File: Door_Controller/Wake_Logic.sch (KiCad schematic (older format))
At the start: 0 parts

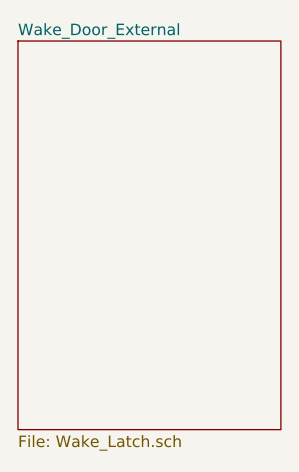
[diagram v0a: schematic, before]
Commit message: complete wake-latch subsheet
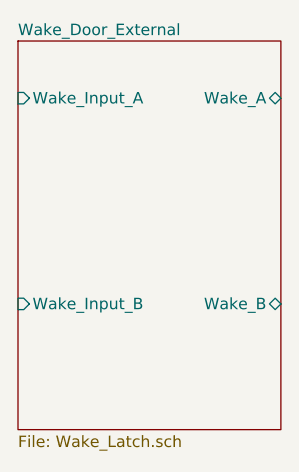
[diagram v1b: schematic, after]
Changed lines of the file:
@@
 F0 "Wake_Door_External" 50
 F1 "Wake_Latch.sch" 50
+F2 "Wake_Input_A" I L 1550 1600 50
+F3 "Wake_Input_B" I L 1550 2500 50
+F4 "Wake_A" B R 2700 1600 50
+F5 "Wake_B" B R 2700 2500 50
 $EndSheet
 $EndSCHEMATC

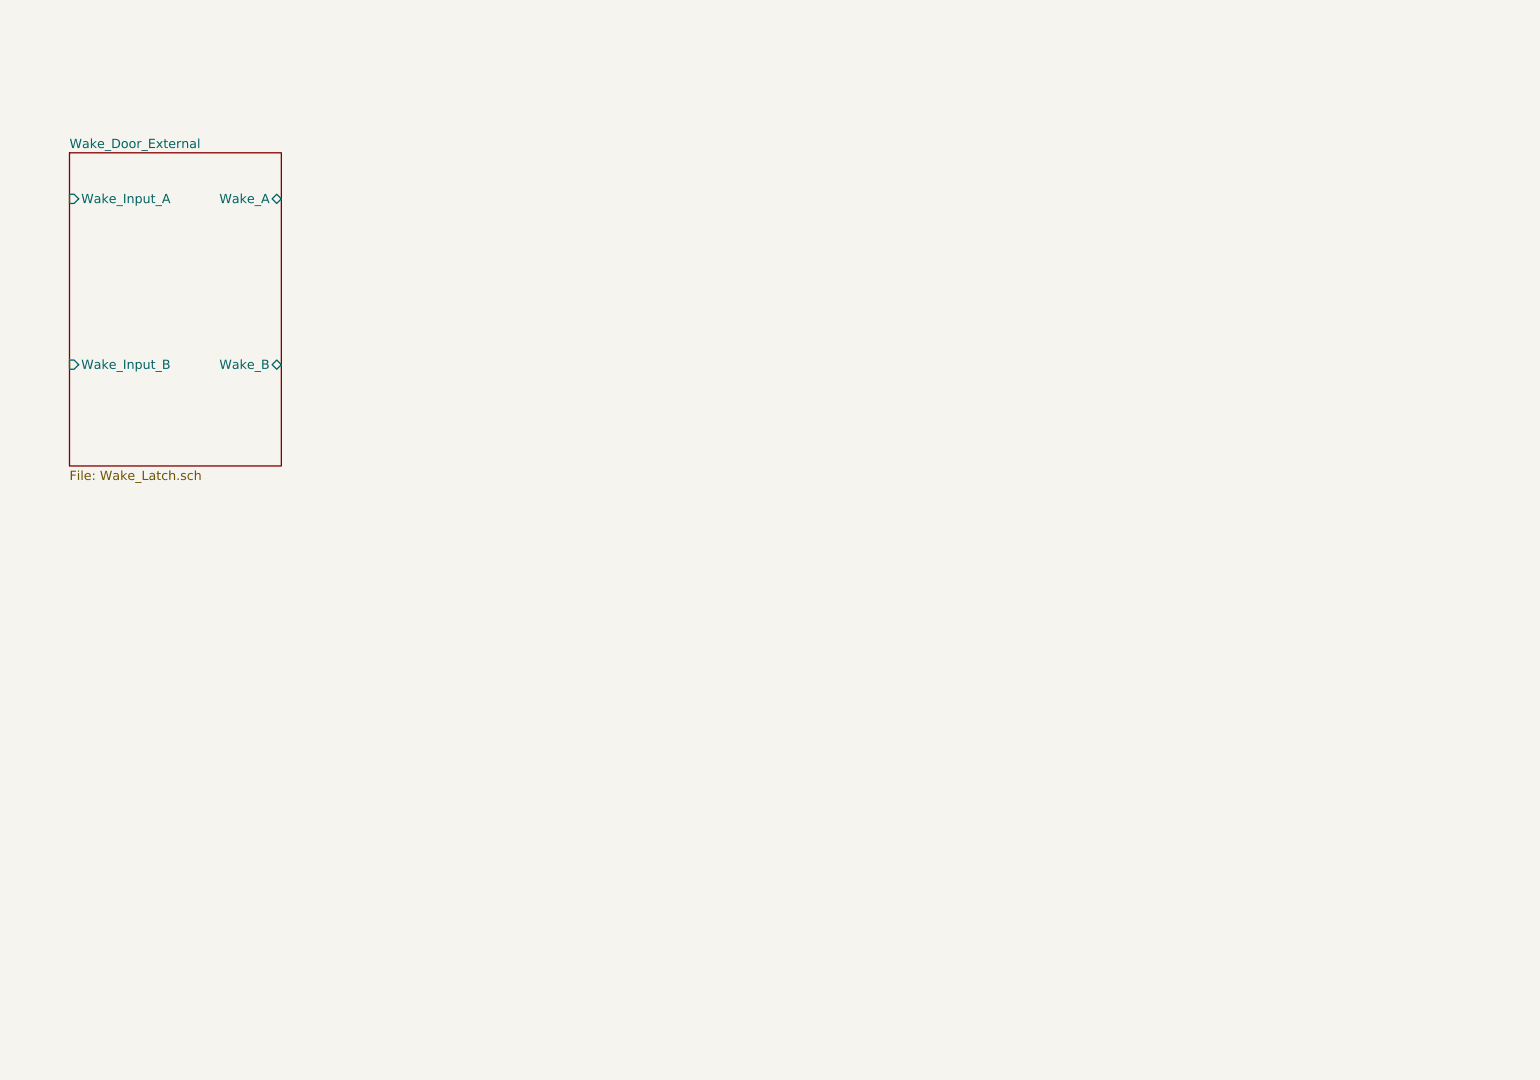
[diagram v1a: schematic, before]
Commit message: Add wake inputs
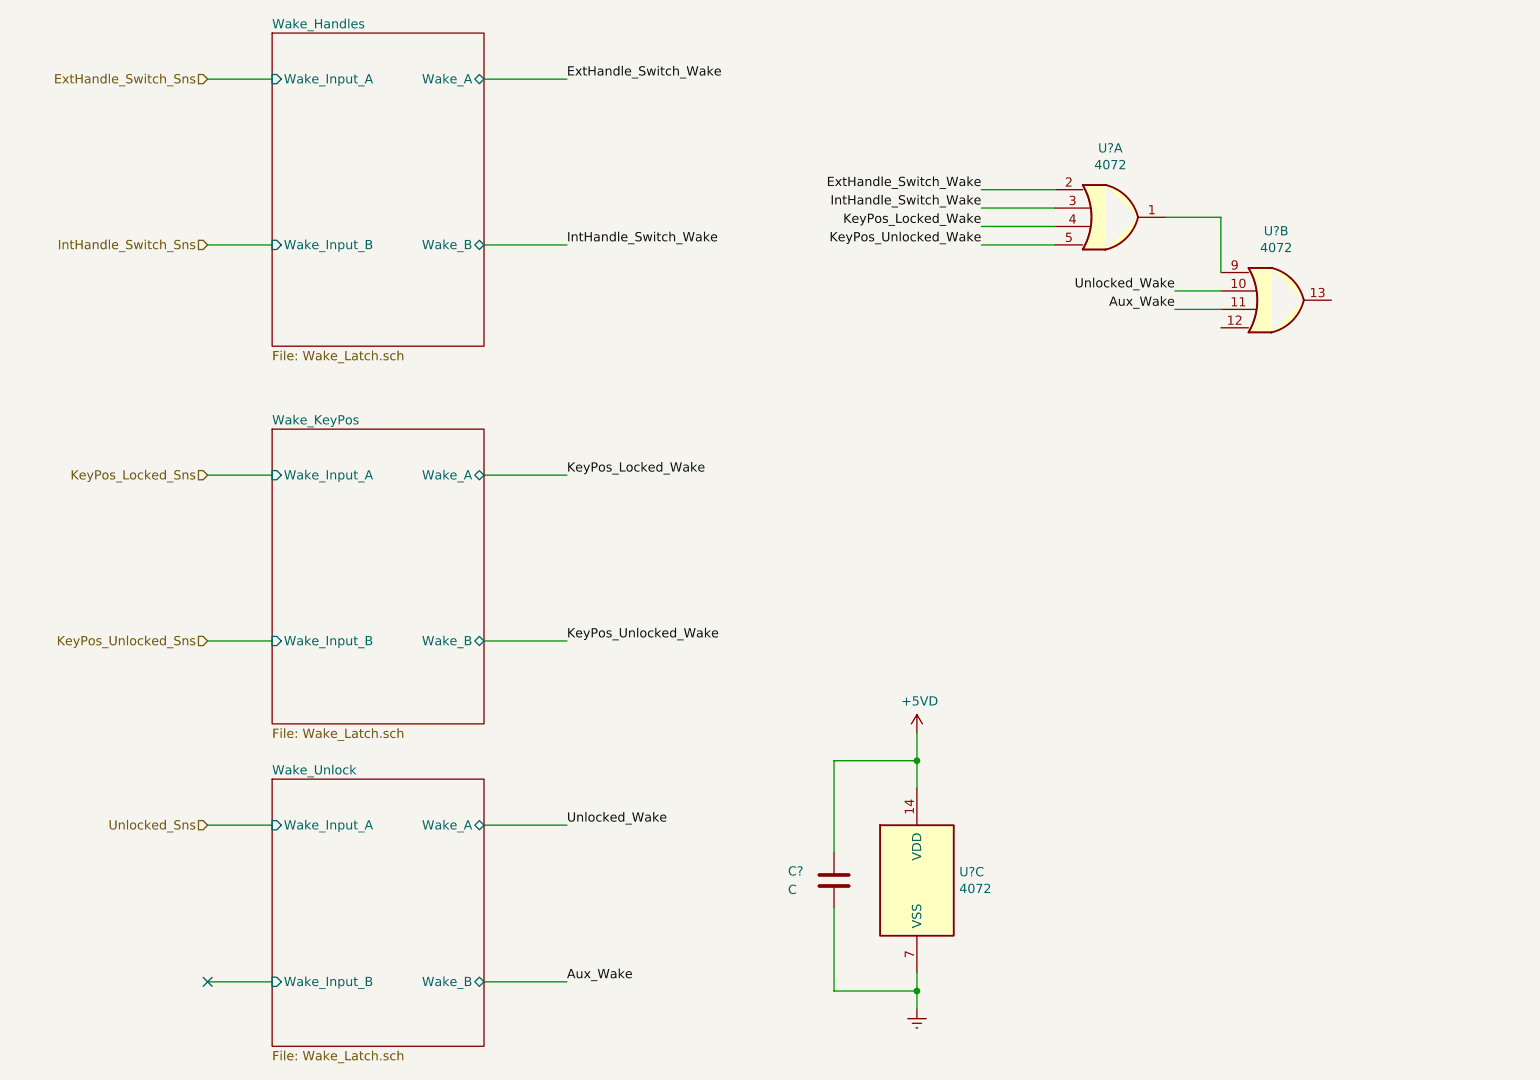
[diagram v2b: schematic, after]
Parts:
- added C?: C, symbol Device:C
- added U? (x3): 4072, symbol 4xxx:4072
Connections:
- new net: U?.1, U?.9
- new net +5VD: C?.1, U?.14 (VDD)
- new net Aux_Wake: U?.11
- new net Earth: C?.2, U?.7 (VSS)
- new net ExtHandle_Switch_Wake: U?.2
- new net IntHandle_Switch_Wake: U?.3
- new net KeyPos_Locked_Wake: U?.4
- new net KeyPos_Unlocked_Wake: U?.5
- new net Unlocked_Wake: U?.10
- no-connect marks 0 -> 1
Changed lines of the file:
@@
 $Descr A4 11693 8268
 encoding utf-8
-Sheet 13 14
+Sheet 13 16
 Title ""
 Date ""
@@
 $EndDescr
 $Sheet
-S 1550 1350 1150 1700
+S 2650 700  1150 1700
 U 60BD8C71
-F0 "Wake_Door_External" 50
+F0 "Wake_Handles" 50
 F1 "Wake_Latch.sch" 50
-F2 "Wake_Input_A" I L 1550 1600 50
-F3 "Wake_Input_B" I L 1550 2500 50
-F4 "Wake_A" B R 2700 1600 50
-F5 "Wake_B" B R 2700 2500 50
+F2 "Wake_Input_A" I L 2650 950 50
+F3 "Wake_Input_B" I L 2650 1850 50
+F4 "Wake_A" B R 3800 950 50
+F5 "Wake_B" B R 3800 1850 50
 $EndSheet
+Text HLabel 2300 950  0    50   Input ~ 0
+ExtHandle_Switch_Sns
+Text HLabel 2300 1850 0    50   Input ~ 0
+IntHandle_Switch_Sns
+Wire Wire Line
+	2300 1850 2650 1850
+Wire Wire Line
+	2300 950  2650 950
+$Sheet
+S 2650 2850 1150 1600
+U 613ABD4B
+F0 "Wake_KeyPos" 50
+F1 "Wake_Latch.sch" 50
+F2 "Wake_Input_A" I L 2650 3100 50
+F3 "Wake_Input_B" I L 2650 4000 50
+F4 "Wake_A" B R 3800 3100 50
+F5 "Wake_B" B R 3800 4000 50
+$EndSheet
+Text HLabel 2300 3100 0    50   Input ~ 0
+KeyPos_Locked_Sns
+Text HLabel 2300 4000 0    50   Input ~ 0
+KeyPos_Unlocked_Sns
+Wire Wire Line
+	2300 4000 2650 4000
+Wire Wire Line
+	2300 3100 2650 3100
+$Sheet
+S 2650 4750 1150 1450
+U 613AC461
+F0 "Wake_Unlock" 50
+F1 "Wake_Latch.sch" 50
+F2 "Wake_Input_A" I L 2650 5000 50
+F3 "Wake_Input_B" I L 2650 5850 50
+F4 "Wake_A" B R 3800 5000 50
+F5 "Wake_B" B R 3800 5850 50
+$EndSheet
+Text HLabel 2300 5000 0    50   Input ~ 0
+Unlocked_Sns
+Wire Wire Line
+	2300 5000 2650 5000
+NoConn ~ 2300 5850
+Wire Wire Line
+	2300 5850 2650 5850
+$Comp
+L 4xxx:4072 U?
+U 1 1 613AD850
+P 7200 1700
+F 0 "U?" H 7200 2075 50  0000 C CNN
+F 1 "4072" H 7200 1984 50  0000 C CNN
+F 2 "" H 7200 1700 50  0001 C CNN
+F 3 "http://www.intersil.com/content/dam/Intersil/documents/cd40/cd4071bms-72bms-75bms.pdf" H 7200 1700 50  0001 C CNN
+	1    7200 1700
+	1    0    0    -1
+$EndComp
+$Comp
+L 4xxx:4072 U?
+U 2 1 613B08A5
+P 8100 2150
+F 0 "U?" H 8100 2525 50  0000 C CNN
+F 1 "4072" H 8100 2434 50  0000 C CNN
+F 2 "" H 8100 2150 50  0001 C CNN
+F 3 "http://www.intersil.com/content/dam/Intersil/documents/cd40/cd4071bms-72bms-75bms.pdf" H 8100 2150 50  0001 C CNN
+	2    8100 2150
+	1    0    0    -1
+$EndComp
+$Comp
+L 4xxx:4072 U?
+U 3 1 613B0DB9
+P 6150 5300
+F 0 "U?" H 6380 5346 50  0000 L CNN
+F 1 "4072" H 6380 5255 50  0000 L CNN
+F 2 "" H 6150 5300 50  0001 C CNN
+F 3 "http://www.intersil.com/content/dam/Intersil/documents/cd40/cd4071bms-72bms-75bms.pdf" H 6150 5300 50  0001 C CNN
+	3    6150 5300
+	1    0    0    -1
+$EndComp
+$Comp
+L power:Earth #PWR?
+U 1 1 613B34D8
+P 6150 6000
+F 0 "#PWR?" H 6150 5750 50  0001 C CNN
+F 1 "Earth" H 6150 5850 50  0001 C CNN
+F 2 "" H 6150 6000 50  0001 C CNN
+F 3 "~" H 6150 6000 50  0001 C CNN
+	1    6150 6000
+	1    0    0    -1
+$EndComp
+$Comp
+L power:+5VD #PWR?
+U 1 1 613B3FE3
+P 6150 4500
+F 0 "#PWR?" H 6150 4350 50  0001 C CNN
+F 1 "+5VD" H 6165 4673 50  0000 C CNN
+F 2 "" H 6150 4500 50  0001 C CNN
+F 3 "" H 6150 4500 50  0001 C CNN
+	1    6150 4500
+	1    0    0    -1
+$EndComp
+$Comp
+L Device:C C?
+U 1 1 613B4A82
+P 5700 5300
+F 0 "C?" H 5450 5350 50  0000 L CNN
+F 1 "C" H 5450 5250 50  0000 L CNN
+F 2 "" H 5738 5150 50  0001 C CNN
+F 3 "~" H 5700 5300 50  0001 C CNN
+	1    5700 5300
+	1    0    0    -1
+$EndComp
+Wire Wire Line
+	6150 4800 6150 4650
+Wire Wire Line
+	6150 5800 6150 5900
+Wire Wire Line
+	5700 5450 5700 5900
+Wire Wire Line
+	5700 5900 6150 5900
+Connection ~ 6150 5900
+Wire Wire Line
+	6150 5900 6150 6000
+Wire Wire Line
+	5700 5150 5700 4650
+Wire Wire Line
+	5700 4650 6150 4650
+Connection ~ 6150 4650
+Wire Wire Line
+	6150 4650 6150 4500
+Text Label 4250 950  0    50   ~ 0
+ExtHandle_Switch_Wake
+Text Label 4250 1850 0    50   ~ 0
+IntHandle_Switch_Wake
+Text Label 4250 3100 0    50   ~ 0
+KeyPos_Locked_Wake
+Text Label 4250 4000 0    50   ~ 0
+KeyPos_Unlocked_Wake
+Text Label 4250 5000 0    50   ~ 0
+Unlocked_Wake
+Text Label 4250 5850 0    50   ~ 0
+Aux_Wake
+Wire Wire Line
+	4250 950  3800 950
+Wire Wire Line
+	4250 1850 3800 1850
+Wire Wire Line
+	4250 3100 3800 3100
+Wire Wire Line
+	3800 4000 4250 4000
+Wire Wire Line
+	3800 5000 4250 5000
+Wire Wire Line
+	3800 5850 4250 5850
+Text Label 6500 1550 2    50   ~ 0
+ExtHandle_Switch_Wake
+Text Label 6500 1650 2    50   ~ 0
+IntHandle_Switch_Wake
+Text Label 6500 1750 2    50   ~ 0
+KeyPos_Locked_Wake
+Text Label 6500 1850 2    50   ~ 0
+KeyPos_Unlocked_Wake
+Text Label 7550 2200 2    50   ~ 0
+Aux_Wake
+Wire Wire Line
+	6900 1550 6500 1550
+Wire Wire Line
+	6500 1650 6900 1650
+Wire Wire Line
+	6500 1750 6900 1750
+Wire Wire Line
+	6500 1850 6900 1850
+Wire Wire Line
+	7500 1700 7800 1700
+Wire Wire Line
+	7800 1700 7800 2000
+Wire Wire Line
+	7550 2100 7800 2100
+Text Label 7550 2100 2    50   ~ 0
+Unlocked_Wake
+Wire Wire Line
+	7550 2200 7800 2200
 $EndSCHEMATC

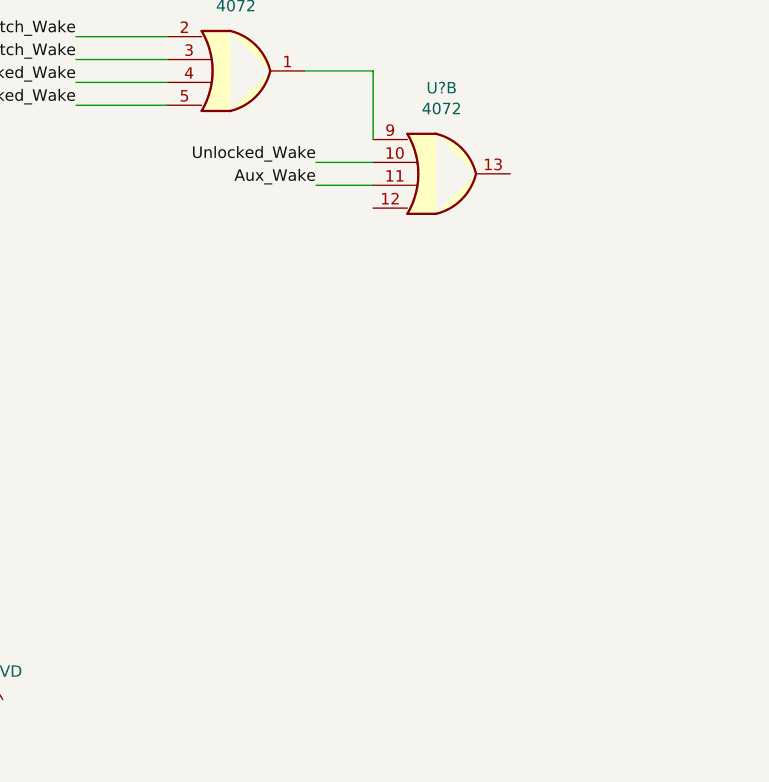
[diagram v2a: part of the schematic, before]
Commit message: simplified wake disable
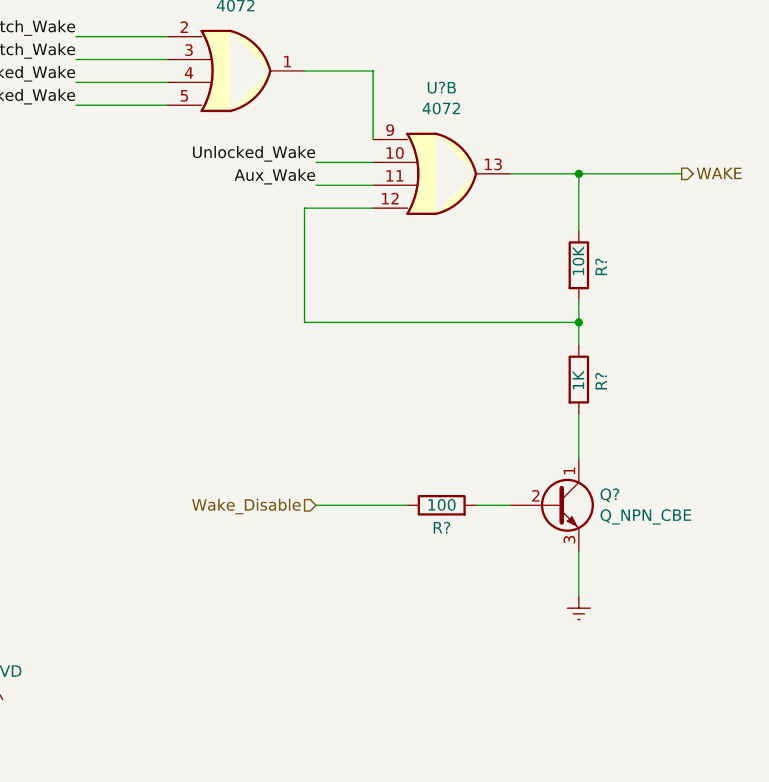
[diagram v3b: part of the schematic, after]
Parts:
- added Q?: Q_NPN_CBE, symbol Device:Q_NPN_CBE
- added R?: 1K, symbol Device:R
- added R?: 100, symbol Device:R
- added R?: 10K, symbol Device:R
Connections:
- net Earth: now also Q?.3 (E)
- net at U?.12: now also R?.1, R?.2
- net WAKE: now reaches U?.13
- net WAKE: now also R?.1
- new net: Q?.1 (C), R?.2
- new net: Q?.2 (B), R?.2
- new net Wake_Disable: R?.1
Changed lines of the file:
@@
 Wire Wire Line
 	7550 2200 7800 2200
+Text HLabel 9150 2150 2    50   Output ~ 0
+WAKE
+$Comp
+L Device:Q_NPN_CBE Q?
+U 1 1 6191434E
+P 8600 3600
+AR Path="/60BD8BC8/60BD8C71/6191434E" Ref="Q?"  Part="1"
+AR Path="/60BD8BC8/613ABD4B/6191434E" Ref="Q?"  Part="1"
+AR Path="/60BD8BC8/613AC461/6191434E" Ref="Q?"  Part="1"
+AR Path="/60BD8BC8/6191434E" Ref="Q?"  Part="1"
+F 0 "Q?" H 8791 3646 50  0000 L CNN
+F 1 "Q_NPN_CBE" H 8791 3555 50  0000 L CNN
+F 2 "" H 8800 3700 50  0001 C CNN
+F 3 "~" H 8600 3600 50  0001 C CNN
+	1    8600 3600
+	1    0    0    -1
+$EndComp
+$Comp
+L Device:R R?
+U 1 1 619258EF
+P 8700 3050
+F 0 "R?" V 8800 3000 50  0000 L CNN
+F 1 "1K" V 8700 3000 50  0000 L CNN
+F 2 "" V 8630 3050 50  0001 C CNN
+F 3 "~" H 8700 3050 50  0001 C CNN
+	1    8700 3050
+	1    0    0    -1
+$EndComp
+$Comp
+L power:Earth #PWR?
+U 1 1 619265B7
+P 8700 4000
+F 0 "#PWR?" H 8700 3750 50  0001 C CNN
+F 1 "Earth" H 8700 3850 50  0001 C CNN
+F 2 "" H 8700 4000 50  0001 C CNN
+F 3 "~" H 8700 4000 50  0001 C CNN
+	1    8700 4000
+	1    0    0    -1
+$EndComp
+$Comp
+L Device:R R?
+U 1 1 6192717C
+P 8100 3600
+F 0 "R?" V 8000 3600 50  0000 C CNN
+F 1 "100" V 8100 3600 50  0000 C CNN
+F 2 "" V 8030 3600 50  0001 C CNN
+F 3 "~" H 8100 3600 50  0001 C CNN
+	1    8100 3600
+	0    -1   -1   0
+$EndComp
+Text HLabel 7550 3600 0    50   Input ~ 0
+Wake_Disable
+Wire Wire Line
+	7550 3600 7950 3600
+Wire Wire Line
+	8250 3600 8400 3600
+Wire Wire Line
+	8700 3400 8700 3200
+Wire Wire Line
+	8700 3800 8700 4000
+Wire Wire Line
+	8400 2150 8700 2150
+$Comp
+L Device:R R?
+U 1 1 61929B15
+P 8700 2550
+F 0 "R?" V 8800 2500 50  0000 L CNN
+F 1 "10K" V 8700 2500 50  0000 L CNN
+F 2 "" V 8630 2550 50  0001 C CNN
+F 3 "~" H 8700 2550 50  0001 C CNN
+	1    8700 2550
+	1    0    0    -1
+$EndComp
+Wire Wire Line
+	8700 2400 8700 2150
+Connection ~ 8700 2150
+Wire Wire Line
+	8700 2150 9150 2150
+Wire Wire Line
+	8700 2700 8700 2800
+Wire Wire Line
+	8700 2800 7500 2800
+Wire Wire Line
+	7500 2800 7500 2300
+Wire Wire Line
+	7500 2300 7800 2300
+Connection ~ 8700 2800
+Wire Wire Line
+	8700 2800 8700 2900
 $EndSCHEMATC
